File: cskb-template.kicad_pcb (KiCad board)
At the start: 6 copper layers, 90.2 x 95.9 mm, 6 parts, among them J1 Conn_02x26_Odd_Even, J2 Conn_02x26_Odd_Even

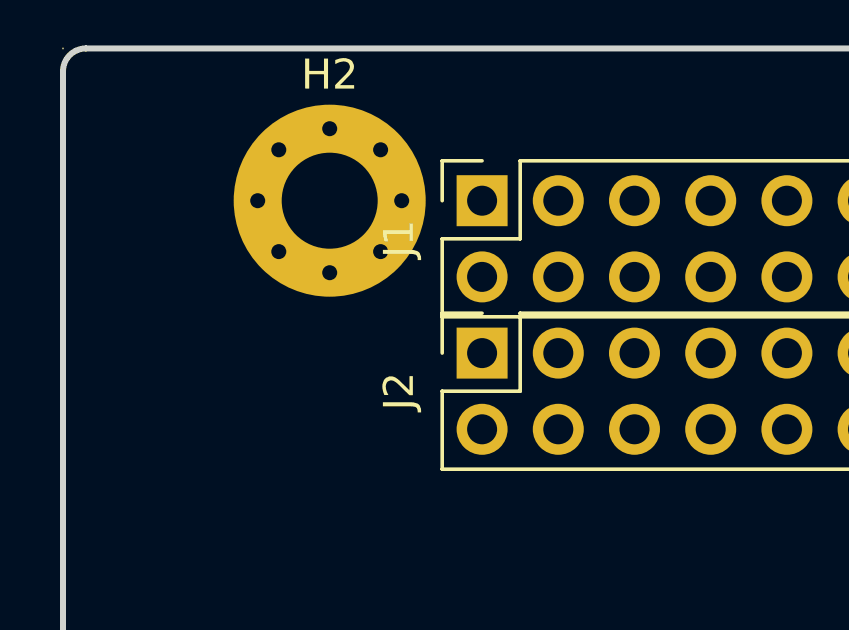
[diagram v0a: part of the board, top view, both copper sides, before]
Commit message: flip CSKB header numbers
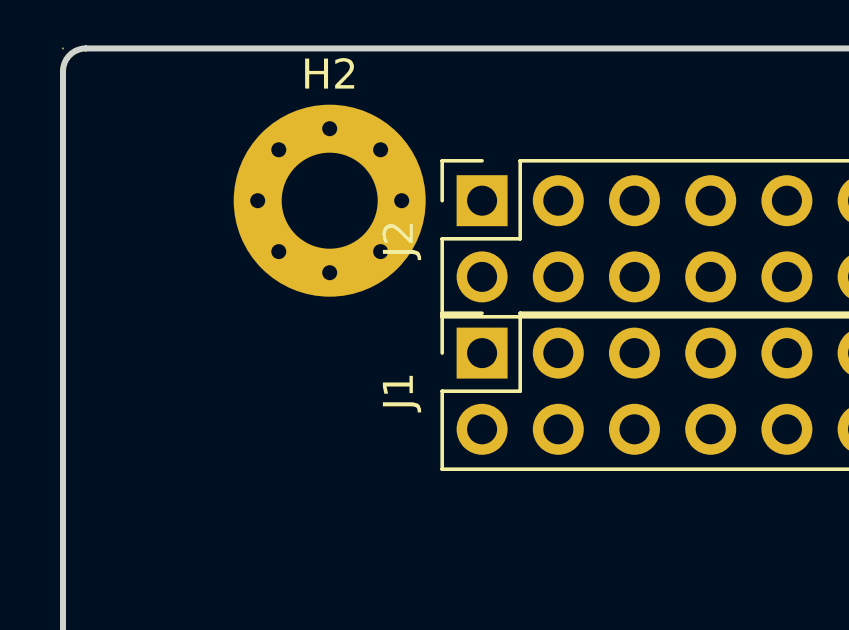
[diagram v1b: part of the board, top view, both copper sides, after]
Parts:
- renumbered J2 to J1, J1 to J2
